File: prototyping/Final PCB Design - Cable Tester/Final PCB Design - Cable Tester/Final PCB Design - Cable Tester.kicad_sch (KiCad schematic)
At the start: 41 parts, among them J1 SFML-110-T1-S-D, J17 Banana Jack, J3 Debug Connection, J4 MEM2061-01-188-00-A_REVA, J5 54-00129, J6 Touchscreen HMI, Q1 MMBT3904, SW1 1x2 Pin header, U1 AVR128DB64x-xMR, U2 LP2985-33DBVR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

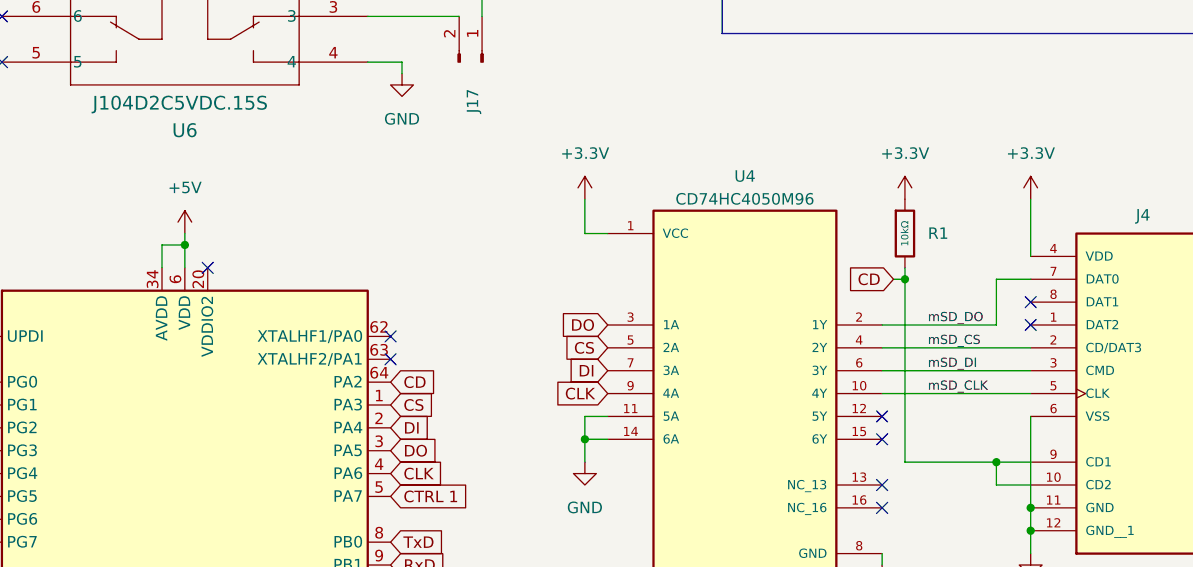
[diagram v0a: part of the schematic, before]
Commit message: Changes to Final board design
Re-routed the DO from microSD to MCU (No more level shifter), added a 5V line to pin 20 so that port C will be powered. Fixed other minor issues after running DRC on layout design.
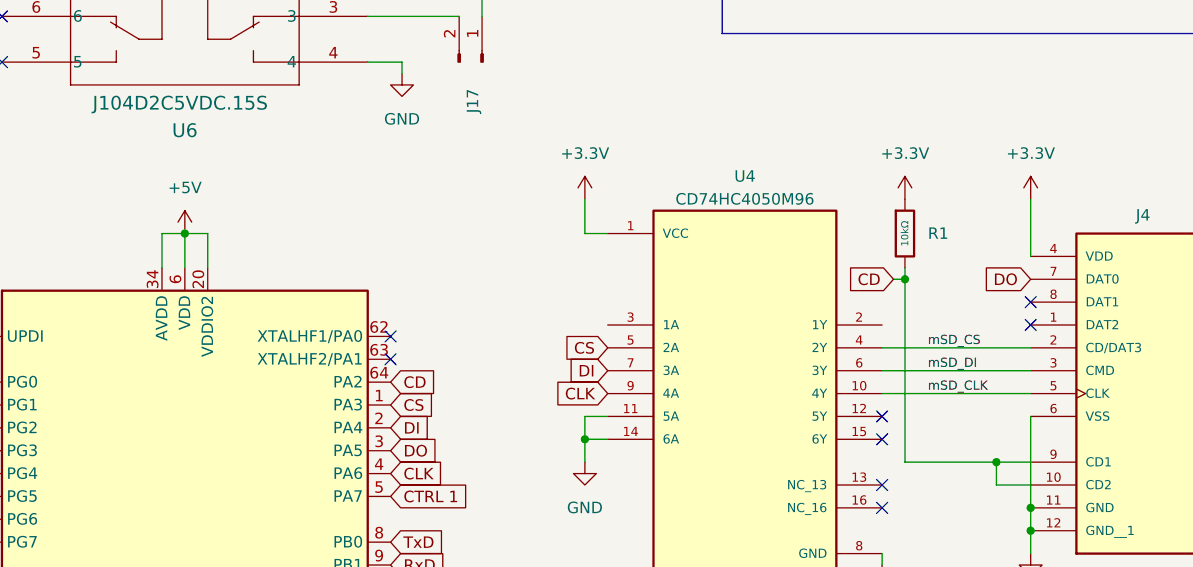
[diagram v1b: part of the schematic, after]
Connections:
- net +5V: now also U1.20 (VDDIO2)
- net DO: now also J4.7 (DAT0); no longer U4.3 (1A)
- net mSD_DO: no longer names the net of U4.2 (1Y)
- net mSD_DO: no longer J4.7 (DAT0)
- no-connect marks 15 -> 14
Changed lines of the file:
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@@
 	)
 	(junction
+		(at 57.15 78.74)
+		(diameter 0)
+		(color 0 0 0 0)
+	)
+	(junction
 		(at 137.16 83.82)
 		(diameter 0)
@@
 	)
 	(junction
-		(at 57.15 80.01)
-		(diameter 0)
-		(color 0 0 0 0)
-	)
-	(junction
 		(at 203.2 110.49)
 		(diameter 0)
@@
 	)
 	(no_connect
-		(at 59.69 82.55)
-	)
-	(no_connect
 		(at 134.62 101.6)
 	)
@@
 	(wire
 		(pts
+			(xy 59.69 78.74) (xy 57.15 78.74)
+		)
+		(stroke
+			(width 0)
+			(type default)
+		)
+	)
+	(wire
+		(pts
 			(xy 190.5 149.86) (xy 194.31 149.86)
 		)
@@
 	(wire
 		(pts
-			(xy 57.15 80.01) (xy 57.15 82.55)
-		)
-		(stroke
-			(width 0)
-			(type default)
-		)
-	)
-	(wire
-		(pts
 			(xy 25.4 36.83) (xy 21.59 36.83)
 		)
@@
 	(wire
 		(pts
+			(xy 59.69 82.55) (xy 59.69 78.74)
+		)
+		(stroke
+			(width 0)
+			(type default)
+		)
+	)
+	(wire
+		(pts
 			(xy 207.01 113.03) (xy 218.44 113.03)
 		)
@@
 	(wire
 		(pts
-			(xy 54.61 82.55) (xy 54.61 80.01)
-		)
-		(stroke
-			(width 0)
-			(type default)
-		)
-	)
-	(wire
-		(pts
 			(xy 271.78 90.17) (xy 267.97 90.17)
 		)
@@
 	(wire
 		(pts
+			(xy 54.61 82.55) (xy 54.61 78.74)
+		)
+		(stroke
+			(width 0)
+			(type default)
+		)
+	)
+	(wire
+		(pts
 			(xy 271.78 119.38) (xy 267.97 119.38)
 		)
@@
 	(wire
 		(pts
-			(xy 134.62 88.9) (xy 147.32 88.9)
-		)
-		(stroke
-			(width 0)
-			(type default)
-		)
-	)
-	(wire
-		(pts
 			(xy 57.15 186.69) (xy 57.15 185.42)
 		)
@@
 	(wire
 		(pts
-			(xy 147.32 88.9) (xy 147.32 83.82)
-		)
-		(stroke
-			(width 0)
-			(type default)
-		)
-	)
-	(wire
-		(pts
 			(xy 212.09 90.17) (xy 203.2 90.17)
 		)
@@
 	(wire
 		(pts
-			(xy 57.15 78.74) (xy 57.15 80.01)
-		)
-		(stroke
-			(width 0)
-			(type default)
-		)
-	)
-	(wire
-		(pts
 			(xy 101.6 101.6) (xy 101.6 104.14)
 		)
@@
 	(wire
 		(pts
-			(xy 147.32 83.82) (xy 151.13 83.82)
-		)
-		(stroke
-			(width 0)
-			(type default)
-		)
-	)
-	(wire
-		(pts
 			(xy 137.16 82.55) (xy 137.16 83.82)
 		)
@@
 	(wire
 		(pts
-			(xy 54.61 80.01) (xy 57.15 80.01)
-		)
-		(stroke
-			(width 0)
-			(type default)
-		)
-	)
-	(wire
-		(pts
 			(xy 170.18 44.45) (xy 170.18 45.72)
 		)
@@
 	(wire
 		(pts
+			(xy 54.61 78.74) (xy 57.15 78.74)
+		)
+		(stroke
+			(width 0)
+			(type default)
+		)
+	)
+	(wire
+		(pts
 			(xy 137.16 83.82) (xy 137.16 104.14)
 		)
@@
 	(wire
 		(pts
+			(xy 57.15 78.74) (xy 57.15 82.55)
+		)
+		(stroke
+			(width 0)
+			(type default)
+		)
+	)
+	(wire
+		(pts
 			(xy 138.43 39.37) (xy 135.89 39.37)
 		)
@@
 		)
 	)
-	(label "mSD_DO"
-		(at 139.7 88.9 0)
-		(effects
-			(font
-				(size 1.016 1.016)
-			)
-			(justify left bottom)
-		)
-	)
 	(label "9V"
 		(at 137.16 36.83 0)
@@
 		)
 	)
+	(global_label "DO"
+		(shape input)
+		(at 151.13 83.82 180)
+		(fields_autoplaced yes)
+		(effects
+			(font
+				(size 1.27 1.27)
+			)
+			(justify right)
+		)
+		(property "Intersheetrefs" "${INTERSHEET_REFS}"
+			(at 145.5443 83.82 0)
+			(effects
+				(font
+					(size 1.27 1.27)
+				)
+				(justify right)
+				(hide yes)
+			)
+		)
+	)
 	(global_label "ADC 2"
 		(shape input)
@@
 		)
 	)
-	(global_label "DO"
-		(shape input)
-		(at 104.14 88.9 180)
-		(fields_autoplaced yes)
-		(effects
-			(font
-				(size 1.27 1.27)
-			)
-			(justify right)
-		)
-		(property "Intersheetrefs" "${INTERSHEET_REFS}"
-			(at 98.5543 88.9 0)
-			(effects
-				(font
-					(size 1.27 1.27)
-				)
-				(justify right)
-				(hide yes)
-			)
-		)
-	)
 	(global_label "CTRL 8"
 		(shape input)
@@
 		(on_board yes)
 		(dnp no)
-		(fields_autoplaced yes)
 		(property "Reference" "#PWR020"
 			(at 57.15 82.55 0)

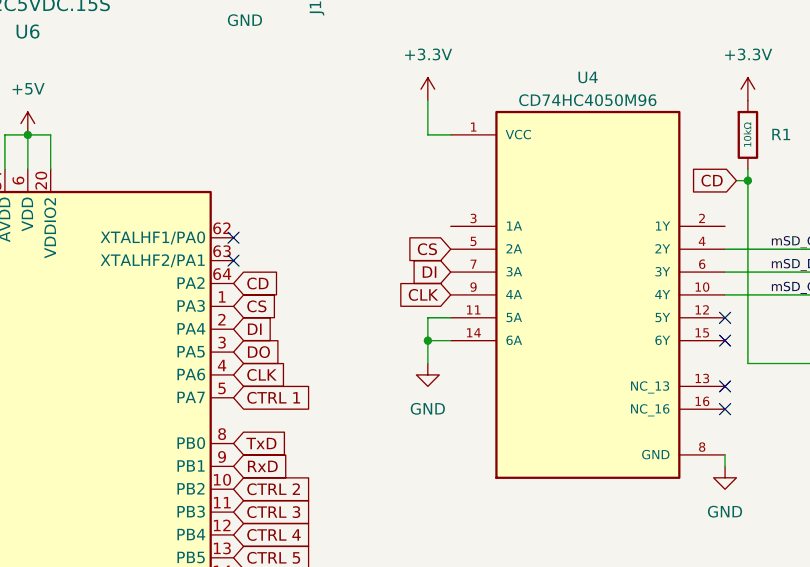
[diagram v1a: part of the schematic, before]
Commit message: Updated final PCB
Tied pin 3 of U4 to GND. Updated the Gerber files for manufacturing.
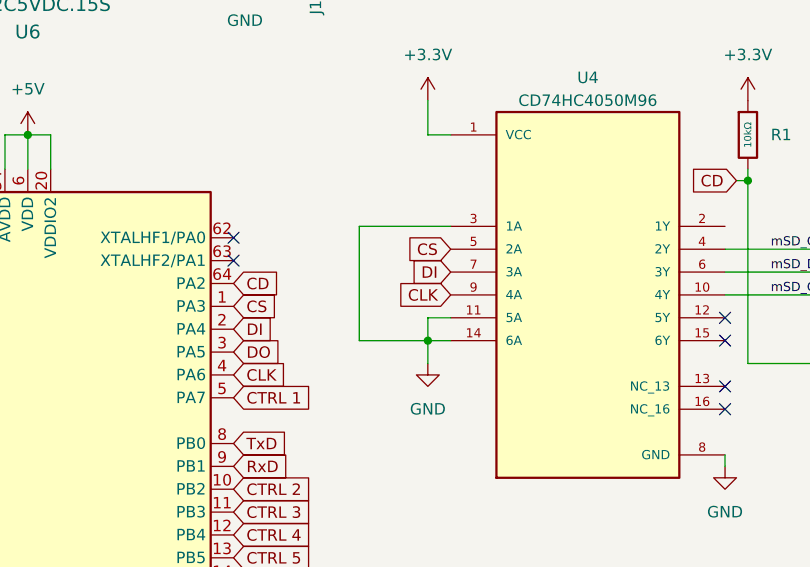
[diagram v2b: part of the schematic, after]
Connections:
- net GND: now also U4.3 (1A)
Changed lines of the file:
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@@
+	(wire
+		(pts
+			(xy 93.98 88.9) (xy 93.98 101.6)
+		)
+		(stroke
+			(width 0)
+			(type default)
+		)
+	)
 	(wire
 		(pts
@@
 	(wire
 		(pts
+			(xy 93.98 101.6) (xy 101.6 101.6)
+		)
+		(stroke
+			(width 0)
+			(type default)
+		)
+	)
+	(wire
+		(pts
 			(xy 214.63 39.37) (xy 212.09 39.37)
 		)
@@
 		)
 		(stroke
+			(width 0)
+			(type default)
+		)
+	)
+	(wire
+		(pts
+			(xy 104.14 88.9) (xy 93.98 88.9)
+		)
+		(stroke
